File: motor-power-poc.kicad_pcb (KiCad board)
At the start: 4 copper layers, 70 x 50 mm, 160 parts, among them J1 Conn_01x04_Pin, J2 USB_C_Receptacle_USB2.0_14P, J3 Conn_01x02, J4 Conn_02x02_Counter_Clockwise, J5 Conn_02x06_Counter_Clockwise, M1 Motor_Servo, M2 Motor_Servo, M3 DC, Q1 Q_NMOS, Q10 Q_NMOS, Q2 Q_NMOS, Q3 Q_NMOS, Q4 Q_NMOS, Q5 Q_NMOS, Q6 Q_NMOS, Q7 Q_NMOS, Q8 Q_NMOS, Q9 Q_NMOS, SW1 SW_Push, SW2 SW_Push, U1 QRE1113GR, U10 CJ431, U11 DRV8701, U2 QRE1113GR, U3 QRE1113GR, U4 ESP32-S3FH4R2, U5 LM74502, U6 TPS5430DDA, U7 TPS56A37, U8 TPS2121, U9 LDL212PV33R, Y1 48M

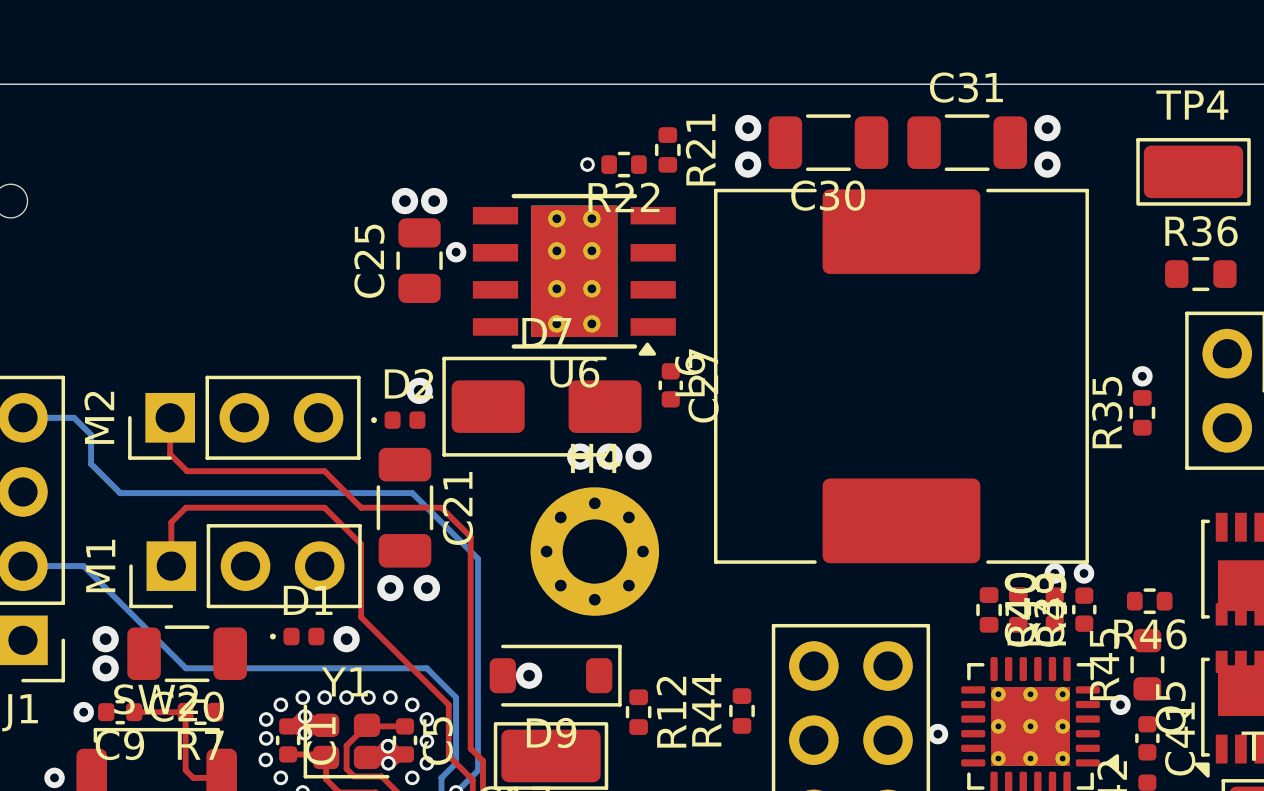
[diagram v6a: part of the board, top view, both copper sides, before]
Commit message: pcb: add TPS5430 routing
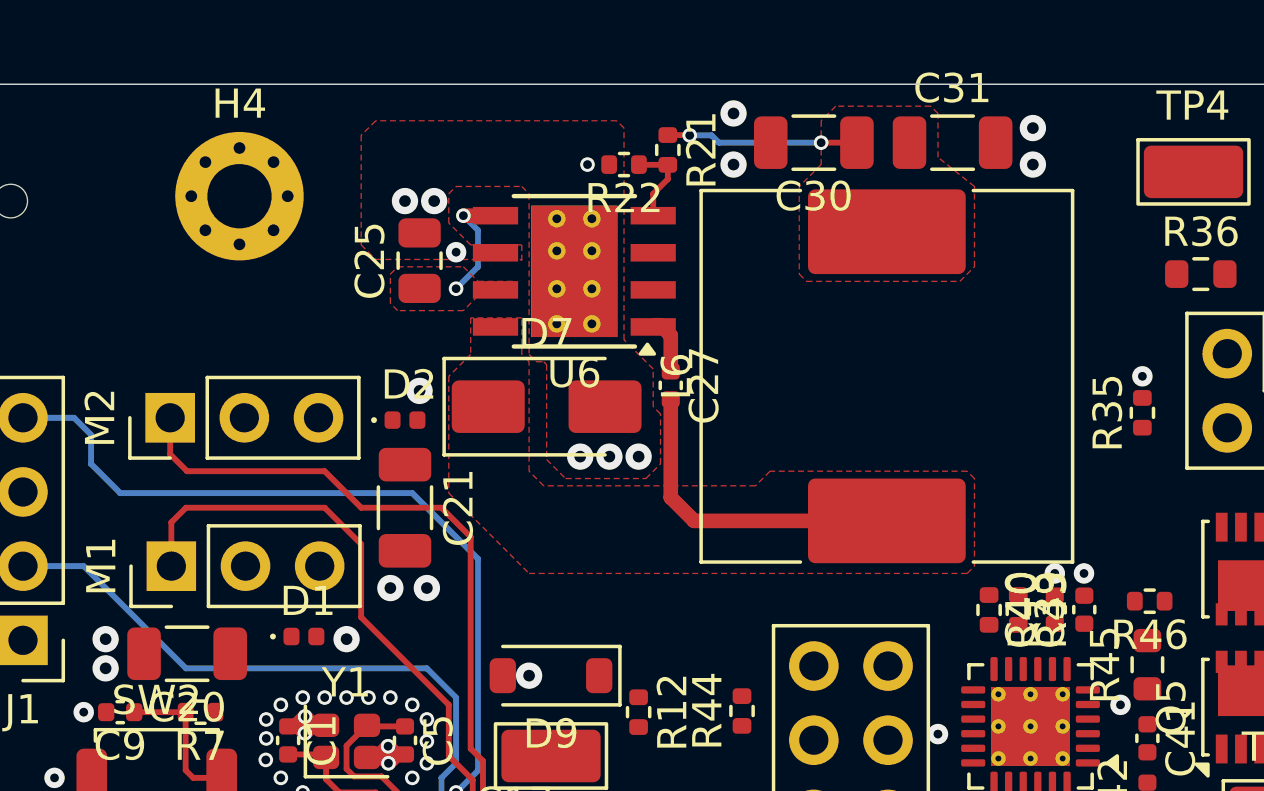
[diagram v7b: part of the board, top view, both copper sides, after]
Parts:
- moved H4 17.2 mm to (126.8, 57.8)
- moved C30 0.50 mm to (146.5, 56.0)
- moved C31 0.50 mm to (151.2, 56.0)
- moved L6 0.50 mm to (149.0, 64.0)
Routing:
- net Net-(D7-K): track 0.00 -> 11.1 mm
- net +5V_buck: track 3.30 -> 9.88 mm, vias 0 -> 2
- net +Vin: track 0.00 -> 4.12 mm, vias 0 -> 2
- net Net-(U6-VSENSE): track 0.00 -> 2.94 mm
- net Net-(U6-BOOT): track 0.00 -> 2.00 mm
- added copper zone on F.Cu, net +5V_buck
- added copper zone on F.Cu, net Net-(D7-K)

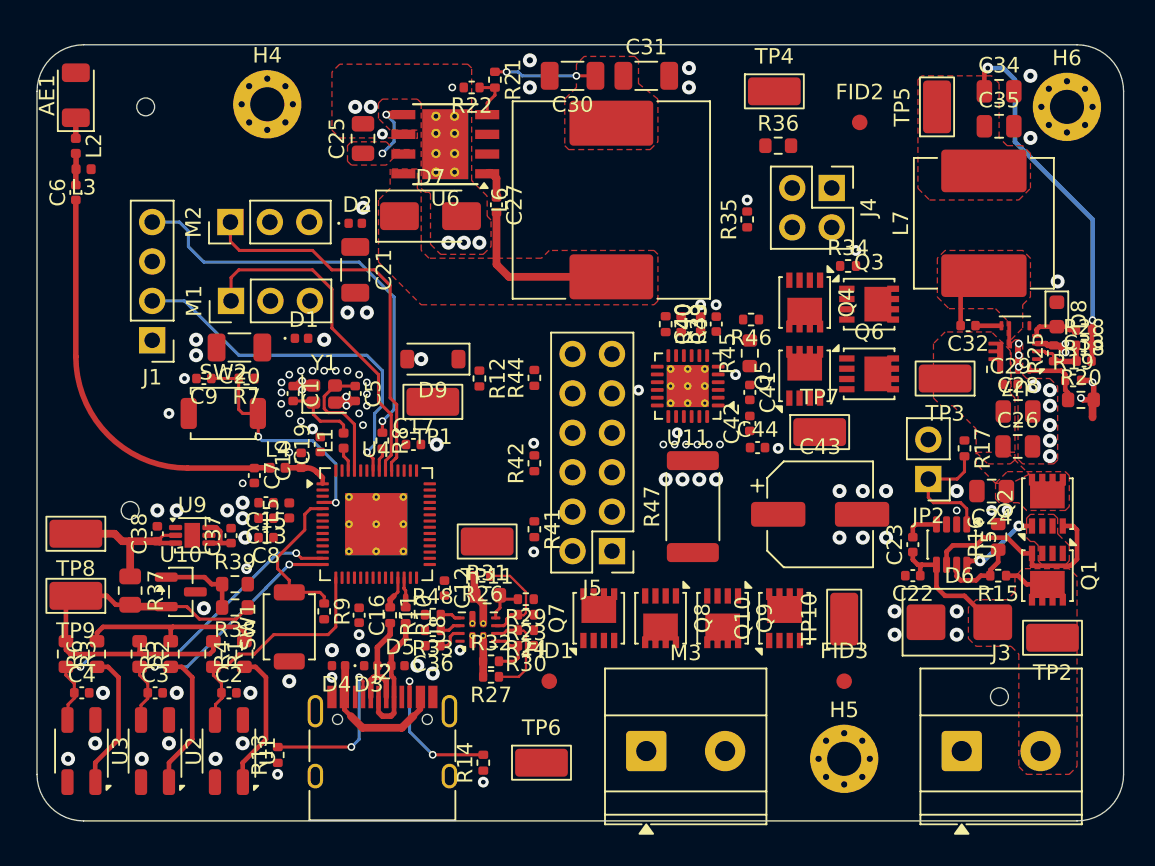
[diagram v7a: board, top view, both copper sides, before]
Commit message: pcb: add Vin selection routing
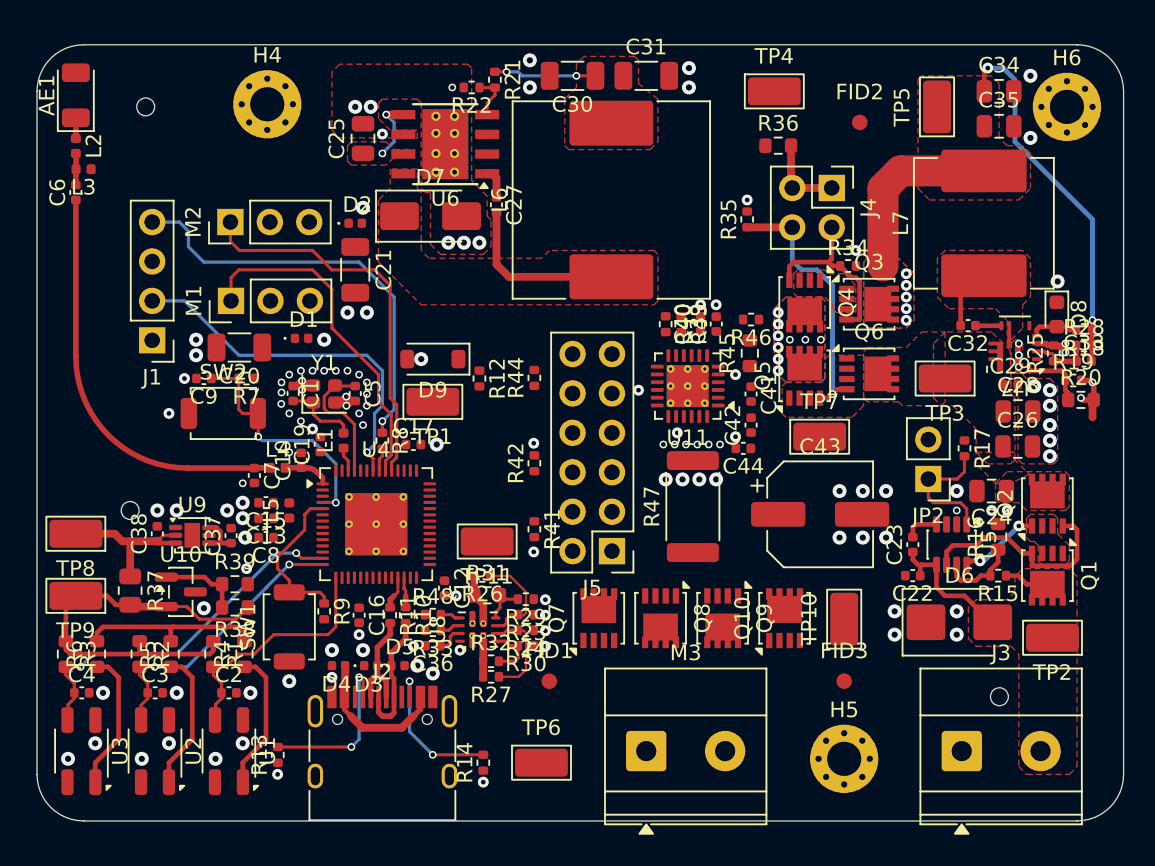
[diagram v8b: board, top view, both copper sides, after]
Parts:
- moved C44 0.92 mm to (157.5, 80.0), turned to 180 degrees
- moved TP7 0.30 mm to (162.4, 79.2)
- moved C41 0.13 mm to (158.0, 76.5)
- moved C42 0.13 mm to (158.0, 78.5)
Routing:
- net Net-(J4-Pin_4): track 0.00 -> 17.3 mm, vias 0 -> 1
- net +12V: track 23.9 -> 35.8 mm, vias 2 -> 7
- net Net-(J4-Pin_2): track 0.00 -> 11.6 mm
- net Net-(J4-Pin_1): track 0.00 -> 5.30 mm
- net GND: vias 118 -> 124
- net /H-bridge/+Vdc: vias 0 -> 9
- added copper zone on B.Cu, net +12V
- added copper zone on B.Cu, net /H-bridge/+Vdc
- added copper zone on F.Cu, net /H-bridge/+Vdc
- added copper zone on F.Cu, net Net-(Q3-S-Pad1)
- added copper zone on F.Cu, net Net-(Q5-S-Pad1)
